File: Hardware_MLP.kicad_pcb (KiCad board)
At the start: 4 copper layers, 70 x 75.1 mm, 738 parts, among them J1 Neuron_Board_Edge, Q1 2SK3018, Q10 2SK3018, Q100 2SK3018, Q101 2SK3018, Q102 2SK3018, Q103 2SK3018, Q104 2SK3018, Q105 2SK3018, Q106 2SK3018, Q107 2SK3018, Q108 2SK3018, Q109 2SK3018, Q11 2SK3018, Q110 2SK3018, Q111 2SK3018, Q112 2SK3018, Q113 2SK3018, Q114 2SK3018, Q115 2SK3018, Q116 2SK3018, Q117 2SK3018, Q118 2SK3018, Q119 2SK3018, Q12 2SK3018, Q120 2SK3018, Q121 2SK3018, Q122 2SK3018, Q123 2SK3018, Q124 2SK3018, Q125 2SK3018, Q126 2SK3018, Q127 2SK3018, Q128 2SK3018, Q129 2SK3018, Q13 2SK3018, Q130 2SK3018, Q131 2SK3018, Q132 2SK3018, Q133 2SK3018, Q134 2SK3018, Q135 2SK3018, Q136 2SK3018, Q137 2SK3018, Q138 2SK3018, Q139 2SK3018, Q14 2SK3018, Q140 2SK3018, Q141 2SK3018, Q142 2SK3018, Q143 2SK3018, Q144 2SK3018, Q145 2SK3018, Q146 2SK3018, Q147 2SK3018, Q148 2SK3018, Q149 2SK3018, Q15 2SK3018, Q150 2SK3018, Q151 2SK3018, Q152 2SK3018, Q153 2SK3018, Q154 2SK3018, Q155 2SK3018, Q156 2SK3018, Q157 2SK3018, Q158 2SK3018, Q159 2SK3018, Q16 2SK3018, Q160 2SK3018, Q161 2SK3018, Q162 2SK3018, Q163 2SK3018, Q164 2SK3018, Q165 2SK3018, Q166 2SK3018, Q167 2SK3018, Q168 2SK3018, Q169 2SK3018, Q17 2SK3018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

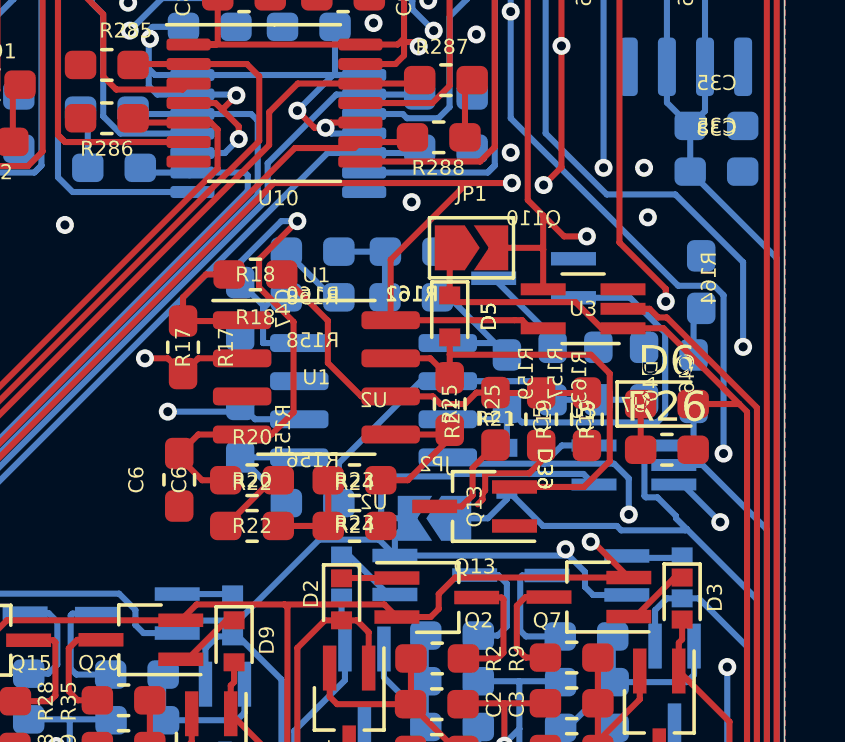
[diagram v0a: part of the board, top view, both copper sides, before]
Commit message: Likely Final Component Values
Most values for components that are not dependent on synapse number have been selected.
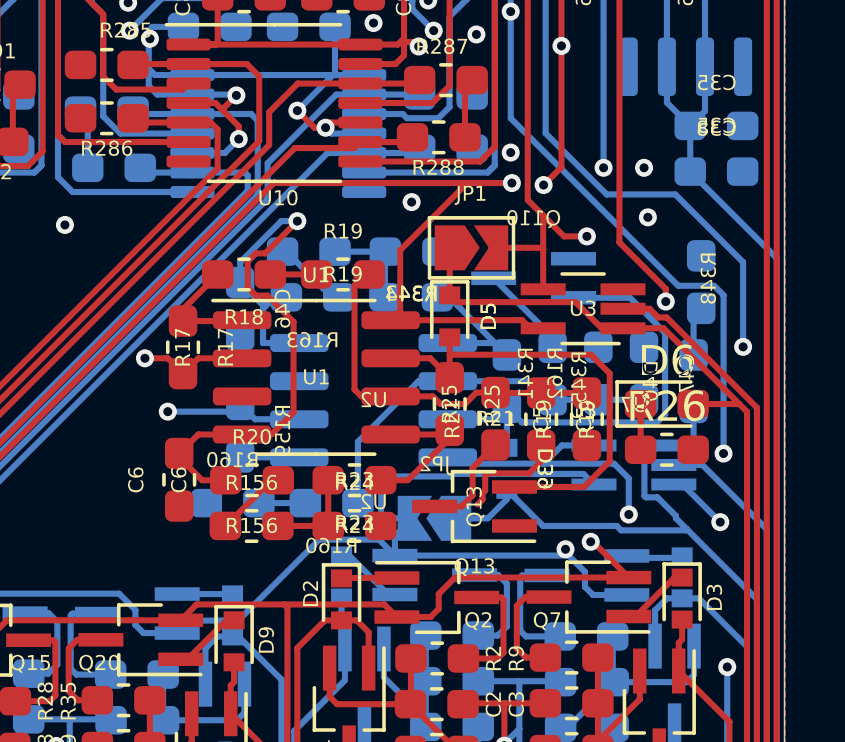
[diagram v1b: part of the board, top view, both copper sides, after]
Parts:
- removed R22: 20K, Resistor_SMD:R_0603_1608Metric_Pad1.05x0.95mm_HandSolder
- added R156: 10K, Resistor_SMD:R_0603_1608Metric_Pad1.05x0.95mm_HandSolder, F.Cu at (135.9, 106.8)
- added R19: 10K, Resistor_SMD:R_0603_1608Metric_Pad1.05x0.95mm_HandSolder, F.Cu at (138.9, 98.4)
- added R342: R_0603_1608Metric_Pad1.05x0.95mm_HandSolder, Resistor_SMD:R_0603_1608Metric_Pad1.05x0.95mm_HandSolder, B.Cu at (137.8, 97.7)
- C1, C10, C11, C12, C13, C14, C15, C16, C17, C18, C19, C2, C20, C21, C22, C23, C24, C25, C26, C27, C28, C29, C3, C30, C31, C32, C33, C34, C4, C42, C43, C44, C45, C48, C49, C50, C51, C52, C53, C54, C55, C56, C57, C58, C59, C60, C61, C62, C63, C64, C65, C66, C67, C68, C69, C7, C70, C71, C72, C73, C74, C75, C8, C9: value C_W -> 10uF
- C46: renamed from C47; value TH_BALL -> .1uF
- C47: renamed from C46; value C_LIF -> 4.7uF
- C5: value C_LIF -> 4.7uF
- C6: value TH_BALL -> .1uF
- D1, D10, D11, D12, D13, D14, D15, D16, D17, D18, D19, D2, D20, D21, D22, D23, D24, D25, D26, D27, D28, D29, D3, D30, D31, D32, D33, D34, D35, D36, D37, D38, D39, D4, D41, D42, D43, D44, D45, D46, D47, D48, D49, D5, D50, D51, D52, D53, D54, D55, D56, D57, D58, D59, D60, D61, D62, D63, D64, D65, D66, D67, D68, D7, D8, D9: value D_Schottky -> RB521S-30
- R1, R10, R100, R107, R108, R115, R116, R123, R124, R131, R132, R139, R140, R147, R148, R165, R166, R173, R174, R181, R182, R189, R190, R197, R198, R2, R205, R206, R213, R214, R221, R222, R229, R230, R237, R238, R245, R246, R253, R254, R261, R262, R269, R27, R270, R28, R35, R36, R43, R44, R51, R52, R59, R60, R67, R68, R75, R76, R83, R84, R9, R91, R92, R99: value R_HEBB -> 100K
- R101, R102, R109, R11, R110, R117, R118, R12, R125, R126, R133, R134, R141, R142, R149, R150, R167, R168, R175, R176, R183, R184, R191, R192, R199, R200, R207, R208, R215, R216, R223, R224, R231, R232, R239, R240, R247, R248, R255, R256, R263, R264, R271, R272, R29, R3, R30, R37, R38, R4, R45, R46, R53, R54, R61, R62, R69, R70, R77, R78, R85, R86, R93, R94: value R_HOMEO -> 100K
- R103, R104, R111, R112, R119, R120, R127, R128, R13, R135, R136, R14, R143, R144, R151, R152, R169, R170, R177, R178, R185, R186, R193, R194, R201, R202, R209, R210, R217, R218, R225, R226, R233, R234, R241, R242, R249, R250, R257, R258, R265, R266, R273, R274, R31, R32, R39, R40, R47, R48, R5, R55, R56, R6, R63, R64, R71, R72, R79, R80, R87, R88, R95, R96: value R_W_LIM -> 1.5K
- R105, R106, R113, R114, R121, R122, R129, R130, R137, R138, R145, R146, R15, R153, R154, R16, R171, R172, R179, R180, R187, R188, R195, R196, R203, R204, R211, R212, R219, R220, R227, R228, R235, R236, R243, R244, R251, R252, R259, R260, R267, R268, R275, R276, R33, R34, R41, R42, R49, R50, R57, R58, R65, R66, R7, R73, R74, R8, R81, R82, R89, R90, R97, R98: value R_TRAIN_PD -> 100K
- R160: value 20K -> Rc
- R160: renamed from R156; value 1K -> Rc
- R163: renamed from R158; value 10K -> 20K
- R18: value 1K -> Rc
- R20: value 10K -> 20K
- R25: value 20K -> 10K
- R345: renamed from R163; value 20K -> 10K
- moved R160 8.41 mm to (138.5, 106.1)
- moved R160 2.67 mm to (135.2, 106.1)
- moved R18 0.38 mm to (135.6, 98.4)
- renumbered R155 to R159, R157 to R162, R159 to R341, R161 to R343, R162 to R344, R164 to R348
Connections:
- C47 pad 1: Net-(C46-Pad1) -> Net-(C47-Pad1)
- R160 pad 1: Net-(R158-Pad2) -> Net-(R160-Pad1)
- R160 pad 2: Net-(R160-Pad2) -> Net-(C47-Pad1)
- R160 pad 1: Net-(C46-Pad1) -> Net-(R160-Pad1)
- R162 pad 2: Net-(C46-Pad1) -> Net-(C47-Pad1)
- R163 pad 2: Net-(R158-Pad2) -> Net-(R163-Pad2)
- R18 pad 1: Net-(C5-Pad1) -> Net-(R18-Pad1)
- R25 pad 1: Net-(D5-Pad2) -> Net-(R158-Pad2)
- R277 pad 1: /X3A -> /X2A
- R278 pad 1: /X4A -> /X1A
- R279 pad 2: /X2A -> /X3A
- R280 pad 2: /X1A -> /X4A
- R313 pad 1: /X6B -> /X7B
- R314 pad 1: /X5B -> /X8B
- R315 pad 2: /X7B -> /X6B
- R316 pad 2: /X8B -> /X5B
- R317 pad 1: /X10B -> /X11B
- R318 pad 1: /X9B -> /X12B
- R319 pad 2: /X11B -> /X10B
- R320 pad 2: /X12B -> /X9B
- R321 pad 1: /X14B -> /X15B
- R322 pad 1: /X13B -> /X16B
- R323 pad 2: /X15B -> /X14B
- R324 pad 2: /X16B -> /X13B
- R325 pad 1: /X18B -> /X19B
- R326 pad 1: /X17B -> /X20B
- R327 pad 2: /X19B -> /X18B
- R328 pad 2: /X20B -> /X17B
- R329 pad 1: /X22B -> /X23B
- R330 pad 1: /X21B -> /X24B
- R331 pad 2: /X23B -> /X22B
- R332 pad 2: /X24B -> /X21B
- R333 pad 1: /X26B -> /X27B
- R334 pad 1: /X25B -> /X28B
- R335 pad 2: /X27B -> /X26B
- R336 pad 2: /X28B -> /X25B
- R337 pad 1: /X30B -> /X31B
- R338 pad 1: /X29B -> /X32B
- R339 pad 2: /X31B -> /X30B
- R340 pad 2: /X32B -> /X29B
- R341 pad 2: Net-(C46-Pad1) -> Net-(C47-Pad1)
- R343 pad 2: Net-(R160-Pad2) -> Net-(R342-Pad2)
- R344 pad 1: Net-(R160-Pad2) -> Net-(R342-Pad2)
- R345 pad 1: Net-(D39-Pad2) -> Net-(R345-Pad1)
- U17 pad 12: /X7B -> /X6B
- U17 pad 2: /X6B -> /X7B
- U17 pad 5: /X5B -> /X8B
- U17 pad 9: /X8B -> /X5B
- U18 pad 12: /X11B -> /X10B
- U18 pad 2: /X10B -> /X11B
- U18 pad 5: /X9B -> /X12B
- U18 pad 9: /X12B -> /X9B
- U19 pad 12: /X15B -> /X14B
- U19 pad 2: /X14B -> /X15B
- U19 pad 5: /X13B -> /X16B
- U19 pad 9: /X16B -> /X13B
- U2 pad 6: Net-(C46-Pad1) -> Net-(C47-Pad1)
- U20 pad 12: /X19B -> /X18B
- U20 pad 2: /X18B -> /X19B
- U20 pad 5: /X17B -> /X20B
- U20 pad 9: /X20B -> /X17B
- U21 pad 12: /X23B -> /X22B
- U21 pad 2: /X22B -> /X23B
- U21 pad 5: /X21B -> /X24B
- U21 pad 9: /X24B -> /X21B
- U22 pad 12: /X27B -> /X26B
- U22 pad 2: /X26B -> /X27B
- U22 pad 5: /X25B -> /X28B
- U22 pad 9: /X28B -> /X25B
- U23 pad 12: /X31B -> /X30B
- U23 pad 2: /X30B -> /X31B
- U23 pad 5: /X29B -> /X32B
- U23 pad 9: /X32B -> /X29B
- U3 pad 5: Vs+ -> VCC
- U7 pad 5: Vs+ -> VCC
- U8 pad 12: /X2A -> /X3A
- U8 pad 2: /X3A -> /X2A
- U8 pad 5: /X4A -> /X1A
- U8 pad 9: /X1A -> /X4A
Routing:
- net Net-(C46-Pad1): track 12.9 -> 0.00 mm
- net Net-(C47-Pad1): track 0.00 -> 12.7 mm
- net Net-(R342-Pad2): track 0.00 -> 3.08 mm
- net Net-(R160-Pad2): track 3.08 -> 0.00 mm
- net Net-(R163-Pad2): track 0.00 -> 2.38 mm
- net Net-(R158-Pad2): track 2.38 -> 0.00 mm
- net /X14B: track 58.4 -> 60.4 mm
- net /X15B: track 57.0 -> 55.0 mm
- net /X11B: track 64.6 -> 62.6 mm
- net /X10B: track 66.6 -> 68.7 mm
- net /X3A: track 18.5 -> 16.6 mm
- net /X2A: track 17.8 -> 19.6 mm
- net /X31B: track 54.5 -> 56.4 mm
- net /X30B: track 55.9 -> 54.1 mm
- net /X5B: track 13.2 -> 15.0 mm
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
